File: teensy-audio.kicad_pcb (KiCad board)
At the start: 2 copper layers, 80 x 140 mm, 43 parts, among them J1 AudioJack2, J2 AudioJack2, J3 Barrel_Jack, J4 Conn_02x08_Odd_Even, J5 Conn_02x08_Odd_Even, J6 Conn_02x05_Odd_Even, J7 Conn_01x04, SW1 RotaryEncoder_Switch, SW2 SW_Push, SW3 SW_Push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

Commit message: added power connectors
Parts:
- added J10: Conn_01x05, Connector_PinHeader_2.54mm:PinHeader_1x05_P2.54mm_Vertical, F.Cu at (170.0, 115.0)
- added J8: Conn_01x04, Connector_PinHeader_2.54mm:PinHeader_1x04_P2.54mm_Vertical, F.Cu at (175.0, 108.0)
- added J9: Conn_02x05_Odd_Even, Connector_PinHeader_2.54mm:PinHeader_2x05_P2.54mm_Vertical, F.Cu at (163.0, 115.0)
- moved J3 4.54 mm to (178.0, 34.0), turned to 180 degrees
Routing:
- net +3.3V: track 18.5 -> 215.6 mm
- net +5V: track 0.00 -> 113.5 mm
- net VCC: track 1.50 -> 114.1 mm
- net SW2: track 6.50 -> 76.2 mm
- net JACK_OUT: track 0.00 -> 61.5 mm
- net POT1: track 2.54 -> 62.7 mm
- net POT2: track 2.54 -> 60.7 mm
- net ENC_SW: track 0.00 -> 55.9 mm
- net SW4: track 6.53 -> 59.7 mm
- net ENC_A: track 0.00 -> 50.6 mm
- net POT4: track 2.54 -> 52.7 mm
- net SW5: track 6.50 -> 56.2 mm
- net POT5: track 3.30 -> 52.1 mm
- net JACK_IN: track 0.00 -> 48.2 mm
- net POT3: track 2.74 -> 48.5 mm
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
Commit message: finished pcb
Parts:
- J1, J2: footprint Connector_Audio:Jack_6.35mm_Neutrik_NMJ4HFD2_Horizontal -> Connector_Audio:Jack_6.35mm_Neutrik_NMJ6HFD2-AU_Horizontal
- J3: footprint Connector_BarrelJack:BarrelJack_CUI_PJ-063AH_Horizontal -> Connector_BarrelJack:BarrelJack_GCT_DCJ200-10-A_Horizontal
- moved J2 24.8 mm to (210.1, 47.6), turned to 90 degrees
- moved J1 24.4 mm to (187.7, 47.5), turned to 90 degrees
- moved J3 1.31 mm to (177.9, 35.3)
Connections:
- J3 pad 1: VCC -> GND
- J3 pad 2: GND -> VCC
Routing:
- net VCC: track 114.1 -> 124.6 mm
- net JACK_OUT: track 61.5 -> 52.2 mm
- net JACK_IN: track 48.2 -> 46.6 mm
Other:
- board text added: "3.3V"
- board text added: "5V"
- board text added: "AUDIO IN"
- board text added: "A_OUT"
- board text added: "GND"
- board text added: "IN"
- board text added: "L_IN_L_GND"
- board text added: "L_IN_R"
- board text added: "L_IN_R_GND"
- board text added: "L_OUT_GND"
- board text added: "L_OUT_R"
- board text added: "MISO"
- board text added: "MOSI"
- board text added: "OUT"
- board text added: "POT1"
- board text added: "POT2"
- board text added: "POT3"
- board text added: "POT4"
- board text added: "POT5"
- board text added: "POT6"
- board text added: "POT7"
- board text added: "POT8"
- board text added: "SCK"
- board text added: "SDSC"
- board text added: "Teensy Audio Effects!! V1"
- board text added: "X"

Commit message: minor
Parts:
- moved C3 4.16 mm to (225.0, 100.6)
- turned C1 to 90 degrees
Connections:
- SW1 pad MP: (no net) -> GND
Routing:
- net +3.3V: track 215.6 -> 74.5 mm
- net VCC: track 124.6 -> 40.4 mm
- net +5V: track 113.5 -> 78.5 mm
- net GND: track 17.8 -> 30.8 mm, vias 0 -> 2
- net POT4: track 52.7 -> 62.2 mm
- net JACK_IN: track 46.6 -> 42.6 mm
- net MISO: track 11.0 -> 7.46 mm
- net Net-(C3-Pad1): track 7.18 -> 4.02 mm
- net Net-(U1B--): track 22.2 -> 20.7 mm
- net Net-(C2-Pad1): track 16.7 -> 15.6 mm
- net POT5: track 52.1 -> 51.1 mm
- net VREF: track 20.2 -> 19.3 mm
- net POT6: track 39.5 -> 38.7 mm, vias 1 -> 0
- net SDCS: track 15.2 -> 14.6 mm
- net SW5: vias 0 -> 1
- added copper zone on F.Cu, net +3.3V
- added copper zone on F.Cu, net +5V
- added copper zone on F.Cu, net VCC
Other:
- board text added: "Teensy Audio Effects!! V2"
- board text removed: "Teensy Audio Effects!! V1"

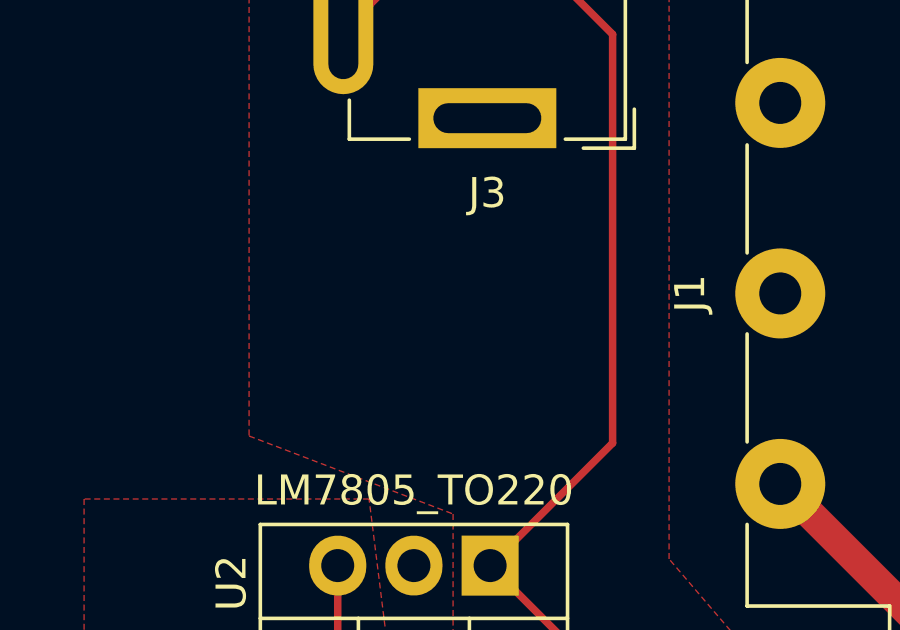
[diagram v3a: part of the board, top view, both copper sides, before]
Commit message: added input power pins
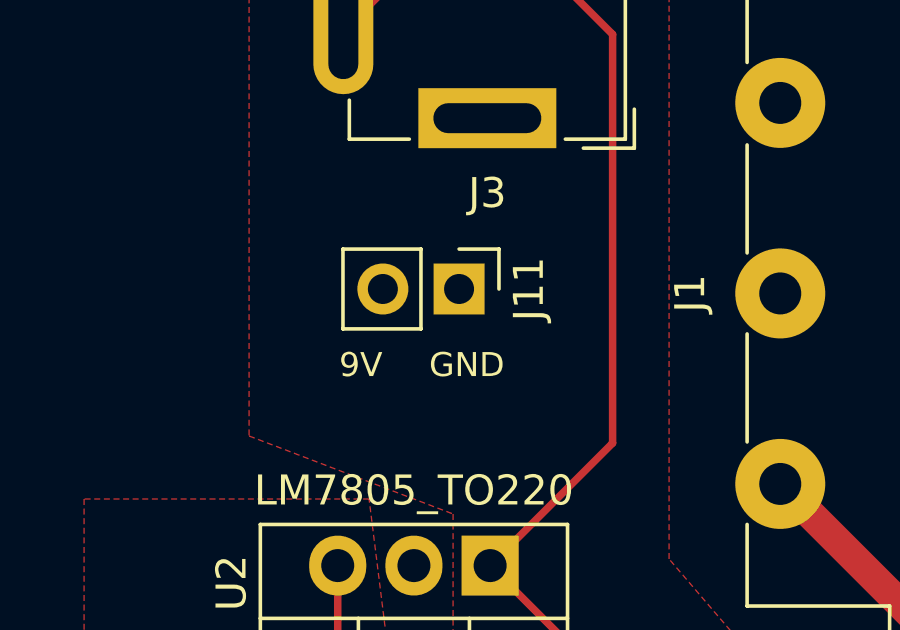
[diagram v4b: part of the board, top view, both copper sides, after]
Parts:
- added J11: Conn_01x02, Connector_PinHeader_2.54mm:PinHeader_1x02_P2.54mm_Vertical, F.Cu at (177.0, 41.0)
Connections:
- J3 pad 3: VCC -> (no net)
- SW1 pad MP: GND -> (no net)
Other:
- board text added: "9V"
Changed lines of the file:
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@@
     )
   )
+  (footprint "Connector_PinHeader_2.54mm:PinHeader_1x02_P2.54mm_Vertical" (layer "F.Cu")
+    (at 177 41 -90)
+    (descr "Through hole straight pin header, 1x02, 2.54mm pitch, single row")
+    (tags "Through hole pin header THT 1x02 2.54mm single row")
+    (property "Sheetfile" "teensy-audio.kicad_sch")
+    (property "Sheetname" "")
+    (property "ki_description" "Generic connector, single row, 01x02, script generated (kicad-library-utils/schlib/autogen/connector/)")
+    (property "ki_keywords" "connector")
+    (attr through_hole)
+    (fp_text reference "J11" (at 0 -2.33 90) (layer "F.SilkS")
+        (effects (font (size 1 1) (thickness 0.15)))
+    )
+    (fp_text value "Conn_01x02" (at 0 4.87 90) (layer "F.Fab")
+        (effects (font (size 1 1) (thickness 0.15)))
+    )
+    (fp_text user "${REFERENCE}" (at 0 1.27) (layer "F.Fab")
+        (effects (font (size 1 1) (thickness 0.15)))
+    )
+    (fp_line (start -1.33 -1.33) (end 0 -1.33)
+      (stroke (width 0.12) (type solid)) (layer "F.SilkS"))
+    (fp_line (start -1.33 0) (end -1.33 -1.33)
+      (stroke (width 0.12) (type solid)) (layer "F.SilkS"))
+    (fp_line (start -1.33 1.27) (end -1.33 3.87)
+      (stroke (width 0.12) (type solid)) (layer "F.SilkS"))
+    (fp_line (start -1.33 1.27) (end 1.33 1.27)
+      (stroke (width 0.12) (type solid)) (layer "F.SilkS"))
+    (fp_line (start -1.33 3.87) (end 1.33 3.87)
+      (stroke (width 0.12) (type solid)) (layer "F.SilkS"))
+    (fp_line (start 1.33 1.27) (end 1.33 3.87)
+      (stroke (width 0.12) (type solid)) (layer "F.SilkS"))
+    (fp_line (start -1.8 -1.8) (end -1.8 4.35)
+      (stroke (width 0.05) (type solid)) (layer "F.CrtYd"))
+    (fp_line (start -1.8 4.35) (end 1.8 4.35)
+      (stroke (width 0.05) (type solid)) (layer "F.CrtYd"))
+    (fp_line (start 1.8 -1.8) (end -1.8 -1.8)
+      (stroke (width 0.05) (type solid)) (layer "F.CrtYd"))
+    (fp_line (start 1.8 4.35) (end 1.8 -1.8)
+      (stroke (width 0.05) (type solid)) (layer "F.CrtYd"))
+    (fp_line (start -1.27 -0.635) (end -0.635 -1.27)
+      (stroke (width 0.1) (type solid)) (layer "F.Fab"))
+    (fp_line (start -1.27 3.81) (end -1.27 -0.635)
+      (stroke (width 0.1) (type solid)) (layer "F.Fab"))
+    (fp_line (start -0.635 -1.27) (end 1.27 -1.27)
+      (stroke (width 0.1) (type solid)) (layer "F.Fab"))
+    (fp_line (start 1.27 -1.27) (end 1.27 3.81)
+      (stroke (width 0.1) (type solid)) (layer "F.Fab"))
+    (fp_line (start 1.27 3.81) (end -1.27 3.81)
+      (stroke (width 0.1) (type solid)) (layer "F.Fab"))
+    (pad "1" thru_hole rect (at 0 0 270) (size 1.7 1.7) (drill 1) (layers "*.Cu" "*.Mask")
+      (net 46 "GND") (pinfunction "Pin_1") (pintype "passive"))
+    (pad "2" thru_hole oval (at 0 2.54 270) (size 1.7 1.7) (drill 1) (layers "*.Cu" "*.Mask")
+      (net 4 "VCC") (pinfunction "Pin_2") (pintype "passive"))
+    (model "${KICAD6_3DMODEL_DIR}/Connector_PinHeader_2.54mm.3dshapes/PinHeader_1x02_P2.54mm_Vertical.wrl"
+      (offset (xyz 0 0 0))
+      (scale (xyz 1 1 1))
+      (rotate (xyz 0 0 0))
+    )
+  )
   (footprint "Resistor_THT:R_Axial_DIN0207_L6.3mm_D2.5mm_P7.62mm_Horizontal" (layer "F.Cu")
     (at 213.36 96.52)
@@
     (pad "C" thru_hole circle (at 0 2.5 270) (size 2 2) (drill 1) (layers "*.Cu" "*.Mask")
       (net 46 "GND") (pinfunction "C") (pintype "passive"))
-    (pad "MP" thru_hole rect (at 7.5 -3.1 270) (size 3.2 2) (drill oval 2.8 1.5) (layers "*.Cu" "*.Mask")
-      (net 46 "GND"))
-    (pad "MP" thru_hole rect (at 7.5 8.1 270) (size 3.2 2) (drill oval 2.8 1.5) (layers "*.Cu" "*.Mask")
-      (net 46 "GND"))
+    (pad "MP" thru_hole rect (at 7.5 -3.1 270) (size 3.2 2) (drill oval 2.8 1.5) (layers "*.Cu" "*.Mask"))
+    (pad "MP" thru_hole rect (at 7.5 8.1 270) (size 3.2 2) (drill oval 2.8 1.5) (layers "*.Cu" "*.Mask"))
     (pad "S1" thru_hole circle (at 14.5 5 270) (size 2 2) (drill 1) (layers "*.Cu" "*.Mask")
       (net 33 "ENC_SW") (pinfunction "S1") (pintype "passive"))
@@
     (pad "2" thru_hole oval (at 0 6.3 180) (size 4.2 2) (drill oval 3.2 1) (layers "*.Cu" "*.Mask")
       (net 4 "VCC") (pintype "passive"))
-    (pad "3" thru_hole oval (at 4.8 2.9 180) (size 2 4.2) (drill oval 1 3.2) (layers "*.Cu" "*.Mask")
-      (net 4 "VCC"))
+    (pad "3" thru_hole oval (at 4.8 2.9 180) (size 2 4.2) (drill oval 1 3.2) (layers "*.Cu" "*.Mask"))
     (model "${KICAD6_3DMODEL_DIR}/Connector_BarrelJack.3dshapes/BarrelJack_GCT_DCJ200-10-A_Horizontal.wrl"
       (offset (xyz 0 0 0))
@@
     (effects (font (size 0.8 0.8) (thickness 0.08)) (justify left bottom))
   )
+  (gr_text "9V" (at 173 44) (layer "F.SilkS")
+    (effects (font (size 0.8 0.8) (thickness 0.08)) (justify left bottom))
+  )
   (gr_text "Teensy Audio\nEffects!!\nV2" (at 169.164 72.39) (layer "F.SilkS")
     (effects (font (size 1.5 1.5) (thickness 0.3) bold) (justify left bottom))
@@
     (effects (font (size 0.8 0.8) (thickness 0.08)) (justify left bottom))
   )
+  (gr_text "GND" (at 176 44) (layer "F.SilkS")
+    (effects (font (size 0.8 0.8) (thickness 0.08)) (justify left bottom))
+  )

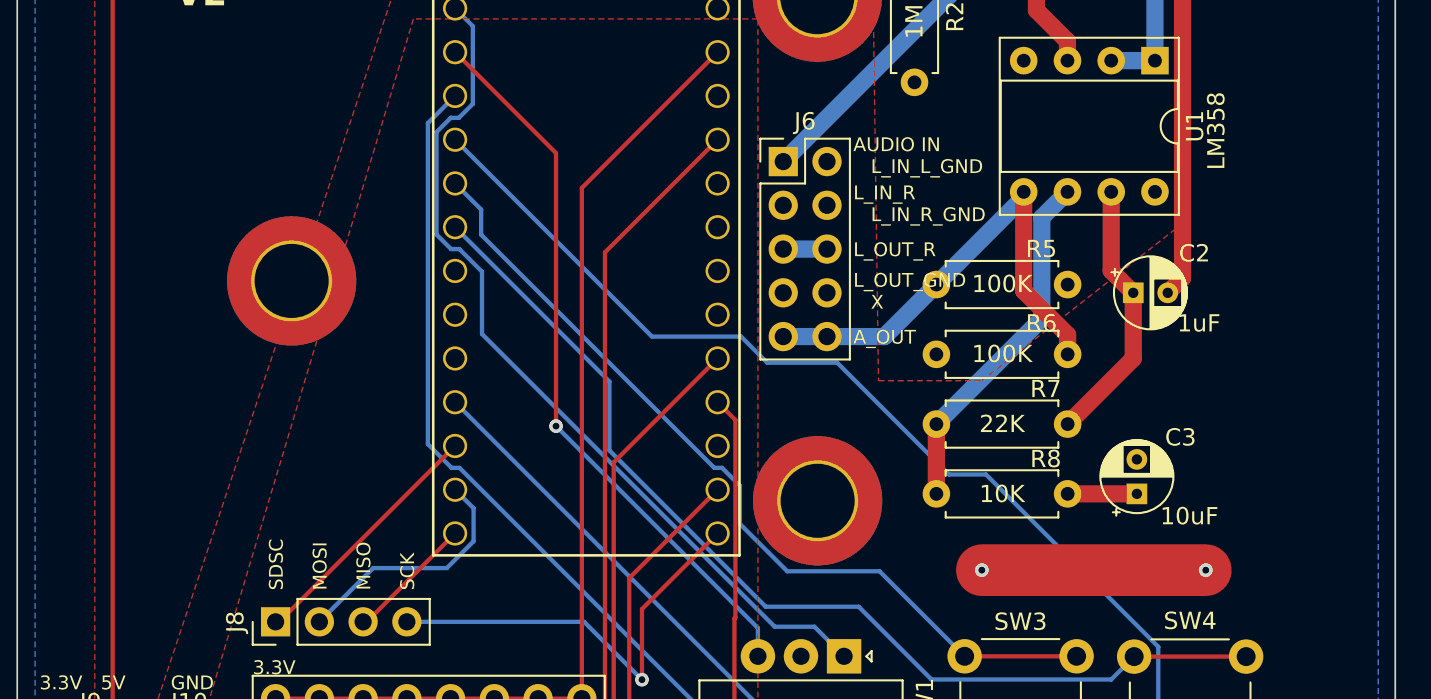
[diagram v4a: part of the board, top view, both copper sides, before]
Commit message: added board dimensions to silkscreen
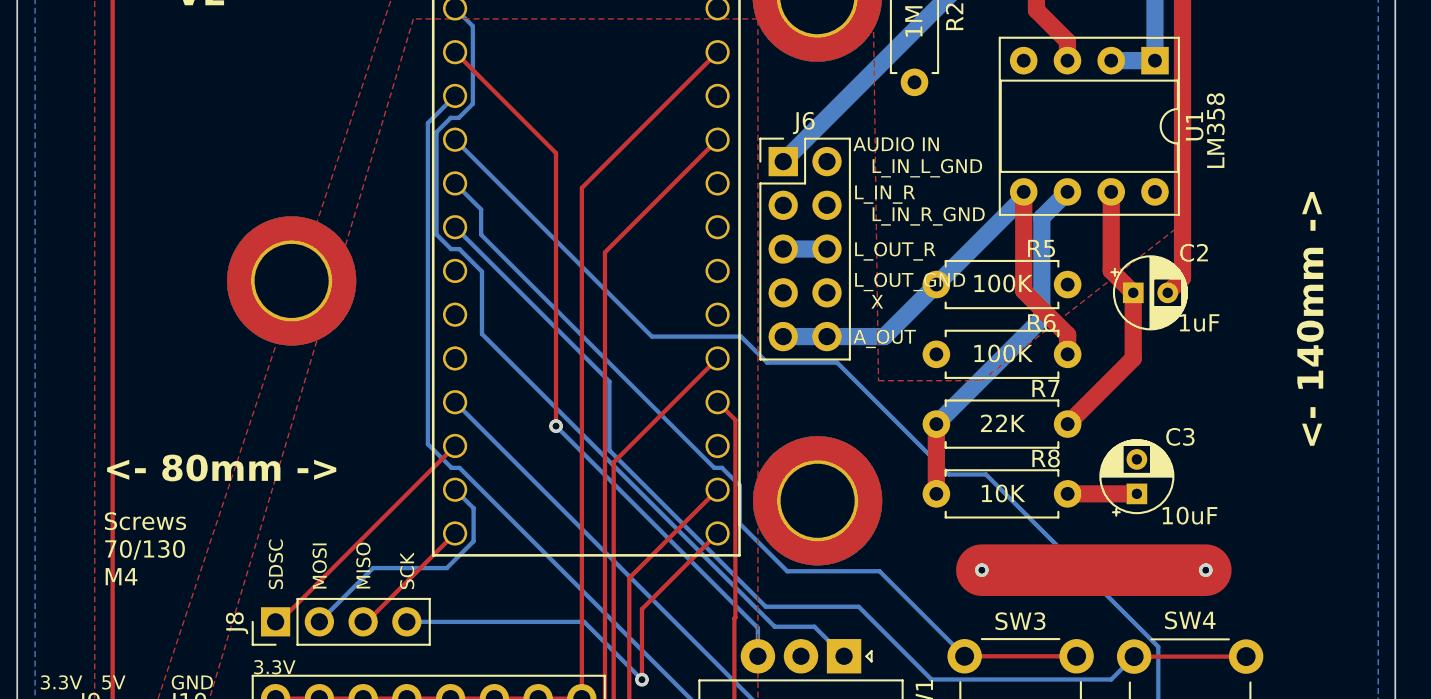
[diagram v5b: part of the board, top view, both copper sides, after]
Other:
- board text added: "<- 140mm ->"
- board text added: "<- 80mm ->"
- board text added: "Screws 70/130 M4"
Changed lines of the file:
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@@
     (effects (font (size 1.5 1.5) (thickness 0.3) bold) (justify left bottom))
+  )
+  (gr_text "Screws\n70/130\nM4" (at 165 106) (layer "F.SilkS")
+    (effects (font (size 1 1) (thickness 0.15)) (justify left bottom))
   )
   (gr_text "GND" (at 168.91 112.014) (layer "F.SilkS")
@@
     (effects (font (size 0.8 0.8) (thickness 0.08)) (justify left bottom))
   )
+  (gr_text "<- 140mm ->" (at 236 98 90) (layer "F.SilkS")
+    (effects (font (size 1.5 1.5) (thickness 0.25) bold) (justify left bottom))
+  )
   (gr_text "POT7" (at 178.054 121.158 90) (layer "F.SilkS")
     (effects (font (size 0.8 0.8) (thickness 0.08)) (justify left bottom))
@@
     (effects (font (size 0.8 0.8) (thickness 0.08)) (justify left bottom))
   )
+  (gr_text "<- 80mm ->" (at 165 100) (layer "F.SilkS")
+    (effects (font (size 1.5 1.5) (thickness 0.25) bold) (justify left bottom))
+  )
   (gr_text "AUDIO IN" (at 208.534 80.772) (layer "F.SilkS")
